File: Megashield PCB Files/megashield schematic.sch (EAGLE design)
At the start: 2 parts

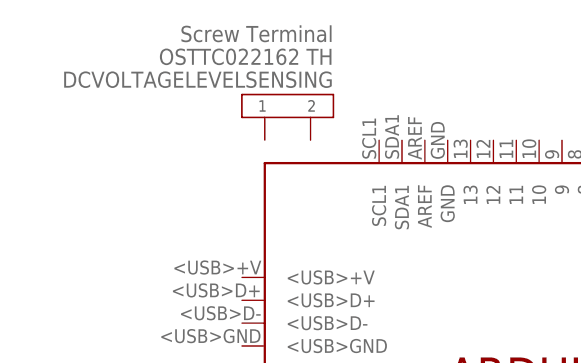
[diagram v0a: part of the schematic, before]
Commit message: Revert "Added Dc Voltage Level Sensor"
This reverts commit 884ff614362a3b5a8655616ef0703b38a716a1fb.
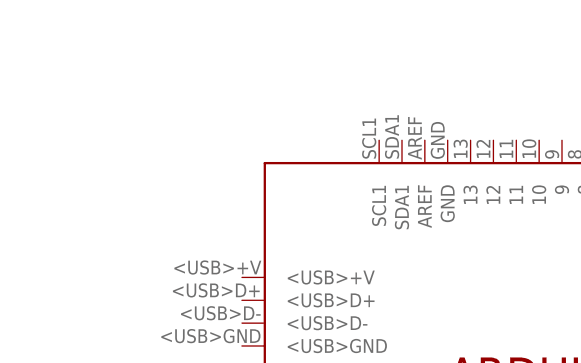
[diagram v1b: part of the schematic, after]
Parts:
- removed DCVOLTAGELEVELSENSING: OSTTC022162_TH, 2-Pin Through-Hole Screw-Terminal:OSTTC022162_TH
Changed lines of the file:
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@@
 <?xml version="1.0" encoding="utf-8"?>
 <!DOCTYPE eagle SYSTEM "eagle.dtd">
-<eagle version="7.7.0">
+<eagle version="7.5.0">
 <drawing>
 <settings>
@@
 <parts>
 <part name="PCB1" library="E14_Arduino_revC" deviceset="ARDUINO_MEGA2560" device=""/>
-<part name="DCVOLTAGELEVELSENSING" library=" 2-Pin Through-Hole Screw-Terminal" deviceset="OSTTC022162_TH" device=""/>
 </parts>
 <sheets>
@@
 <instances>
 <instance part="PCB1" gate="G$1" x="71.12" y="58.42"/>
-<instance part="DCVOLTAGELEVELSENSING" gate="G$1" x="15.24" y="88.9" rot="R180"/>
 </instances>
 <busses>

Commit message: Added Dc Voltage Level Sensor
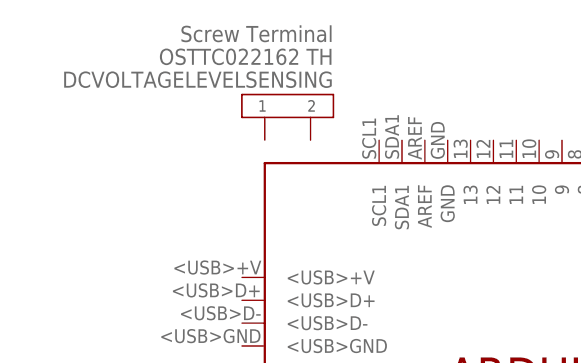
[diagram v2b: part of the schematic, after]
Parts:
- added DCVOLTAGELEVELSENSING: OSTTC022162_TH, 2-Pin Through-Hole Screw-Terminal:OSTTC022162_TH
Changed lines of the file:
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@@
 <?xml version="1.0" encoding="utf-8"?>
 <!DOCTYPE eagle SYSTEM "eagle.dtd">
-<eagle version="7.5.0">
+<eagle version="7.7.0">
 <drawing>
 <settings>
@@
 <parts>
 <part name="PCB1" library="E14_Arduino_revC" deviceset="ARDUINO_MEGA2560" device=""/>
+<part name="DCVOLTAGELEVELSENSING" library=" 2-Pin Through-Hole Screw-Terminal" deviceset="OSTTC022162_TH" device=""/>
 </parts>
 <sheets>
@@
 <instances>
 <instance part="PCB1" gate="G$1" x="71.12" y="58.42"/>
+<instance part="DCVOLTAGELEVELSENSING" gate="G$1" x="15.24" y="88.9" rot="R180"/>
 </instances>
 <busses>
